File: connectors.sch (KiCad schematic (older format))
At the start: 40 parts, among them J10 Conn_01x01, J11 Conn_01x01, J12 Conn_01x01, J13 Conn_01x01, J14 Conn_01x01, J15 Conn_01x01, J16 Conn_01x01, J17 Conn_01x01, J18 Conn_01x01, J19 GND for the Servo connectors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

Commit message: Fix BMP388 footprint issue
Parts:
- R7: value R -> 10k
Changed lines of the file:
@@
 EESchema Schematic File Version 4
+LIBS:kapukiTRX-hw-trx-cache
 EELAYER 30 0
 EELAYER END
@@
 P 3150 4400
 F 0 "R7" H 2950 4450 50  0000 L CNN
-F 1 "R" H 2950 4350 50  0000 L CNN
+F 1 "10k" H 2950 4350 50  0000 L CNN
 F 2 "Resistor_SMD:R_0402_1005Metric" V 3080 4400 50  0001 C CNN
 F 3 "~" H 3150 4400 50  0001 C CNN

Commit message: Final changes for rev.3
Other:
- note added: "CAN interface"
- note added: "Servo 1"
- note added: "Servo 2"
- note added: "Servo 3"
- note added: "Servo 4"
- note added: "Servo 5"
- note added: "Servo 6"
- note added: "Servo 7"
- note added: "Servo 8"
- note added: "Servo connectors"
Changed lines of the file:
@@
 Sheet 2 4
 Title "kapukiTRX - CAN, servro connectors"
-Date "2019-11-09"
-Rev "2"
+Date "2020-01-01"
+Rev "3"
 Comp "bodrico.com"
 Comment1 "Designed by bodri@bodrico.com"
@@
 	1    0    0    -1
 $EndComp
+Text Notes 5550 2450 0    50   ~ 0
+Servo 1
+Text Notes 5550 2900 0    50   ~ 0
+Servo 2
+Text Notes 5550 3350 0    50   ~ 0
+Servo 3
+Text Notes 5550 3800 0    50   ~ 0
+Servo 4
+Text Notes 5550 4250 0    50   ~ 0
+Servo 5
+Text Notes 5550 4700 0    50   ~ 0
+Servo 6
+Text Notes 5550 5150 0    50   ~ 0
+Servo 7
+Text Notes 5550 5600 0    50   ~ 0
+Servo 8
+Wire Notes Line
+	7000 6400 7000 2900
+Wire Notes Line
+	7000 2900 11100 2900
+Text Notes 8750 5850 0    50   ~ 0
+CAN interface
+Text Notes 3900 6950 0    50   ~ 0
+Servo connectors
 $EndSCHEMATC

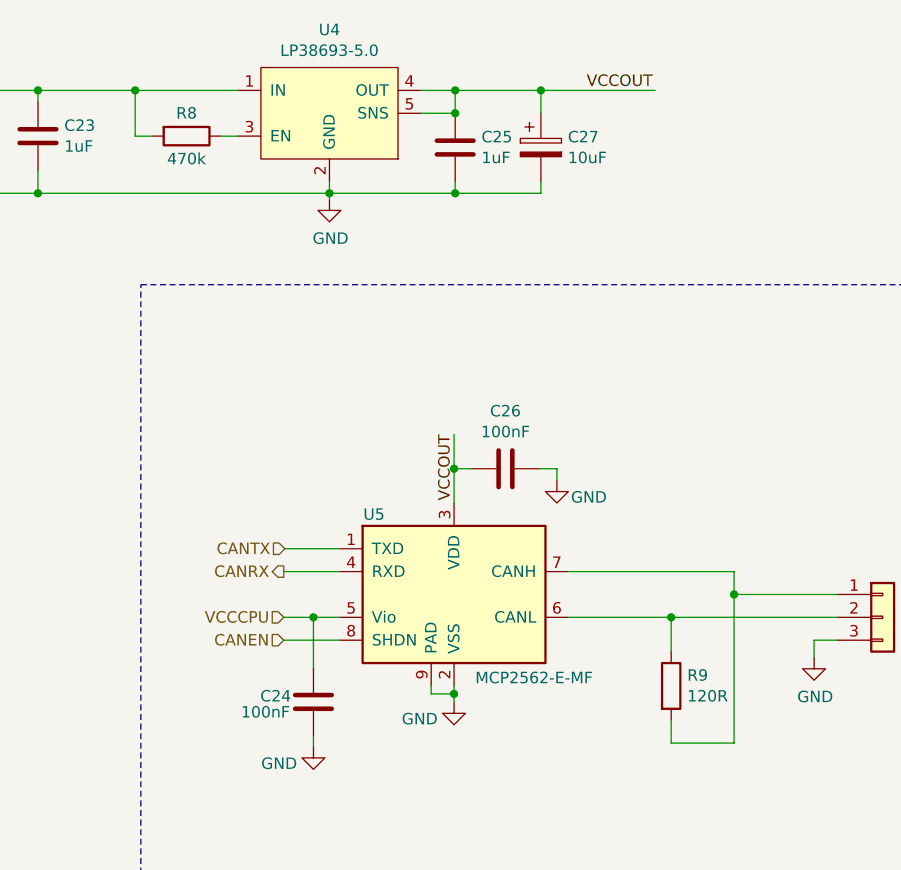
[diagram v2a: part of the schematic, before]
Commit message: Add boot resistor, and fix CAN RX pin
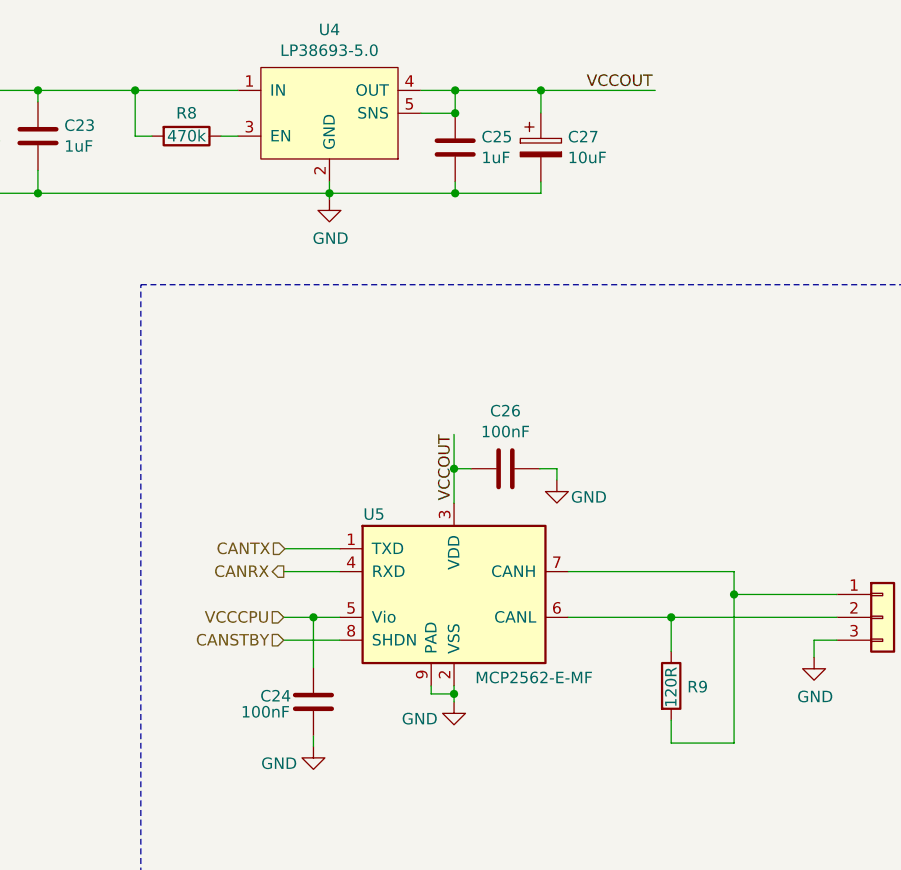
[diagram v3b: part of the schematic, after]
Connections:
- net CANEN renamed CANSTBY
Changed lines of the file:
@@
 Sheet 2 4
 Title "kapukiTRX - CAN, servro connectors"
-Date "2020-01-01"
-Rev "3"
+Date "2020-03-29"
+Rev "4"
 Comp "bodrico.com"
 Comment1 "Designed by bodri@bodrico.com"
@@
 AR Path="/5CCDDFD0" Ref="R?"  Part="1"
 AR Path="/5C76B390/5CCDDFD0" Ref="R9"  Part="1"
-F 0 "R9" H 9390 4701 50  0000 L CNN
-F 1 "120R" H 9390 4610 50  0000 L CNN
+F 0 "R9" H 9390 4650 50  0000 L CNN
+F 1 "120R" V 9320 4560 50  0000 L CNN
 F 2 "Resistor_SMD:R_0402_1005Metric" V 9250 4655 50  0001 C CNN
 F 3 "~" H 9320 4655 50  0001 C CNN
@@
 P 7200 2250
 F 0 "R8" V 7100 2250 50  0000 C CNN
-F 1 "470k" V 7300 2250 50  0000 C CNN
+F 1 "470k" V 7200 2250 50  0000 C CNN
 F 2 "Resistor_SMD:R_0402_1005Metric" V 7130 2250 50  0001 C CNN
 F 3 "~" H 7200 2250 50  0001 C CNN
@@
 	7625 4355 7755 4355
 Text HLabel 7625 4455 0    50   Input ~ 0
-CANEN
+CANSTBY
 Wire Wire Line
 	7625 4455 7870 4455

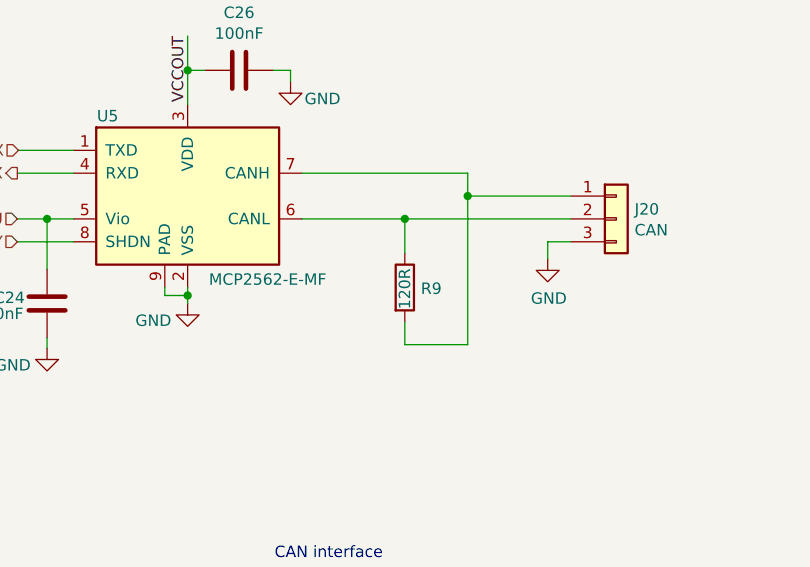
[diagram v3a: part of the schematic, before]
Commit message: Add pull-up for uart
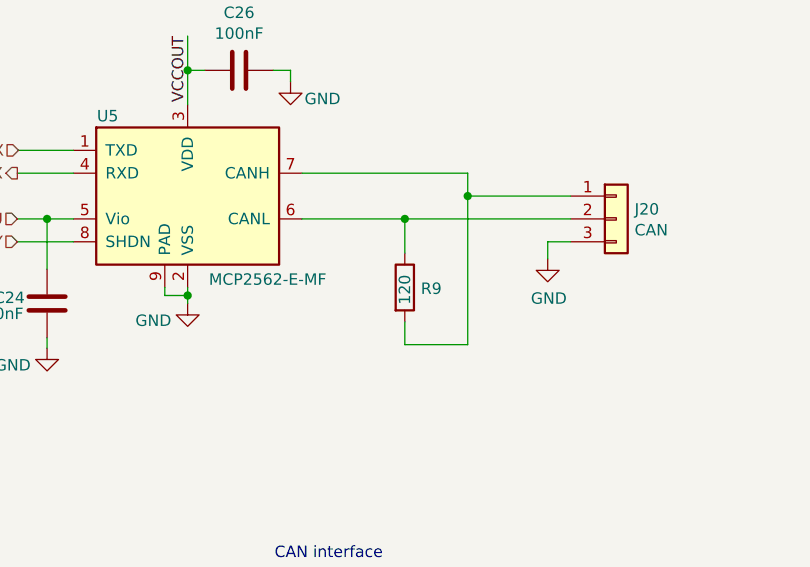
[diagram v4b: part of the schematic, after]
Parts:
- R9: value 120R -> 120
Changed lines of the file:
@@
 AR Path="/5C76B390/5CCDDFD0" Ref="R9"  Part="1"
 F 0 "R9" H 9390 4650 50  0000 L CNN
-F 1 "120R" V 9320 4560 50  0000 L CNN
+F 1 "120" V 9320 4580 50  0000 L CNN
 F 2 "Resistor_SMD:R_0402_1005Metric" V 9250 4655 50  0001 C CNN
 F 3 "~" H 9320 4655 50  0001 C CNN
